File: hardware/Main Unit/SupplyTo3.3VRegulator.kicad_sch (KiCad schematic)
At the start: 22 parts, among them U15 INA180A3, U16 TPS56A37RPAR

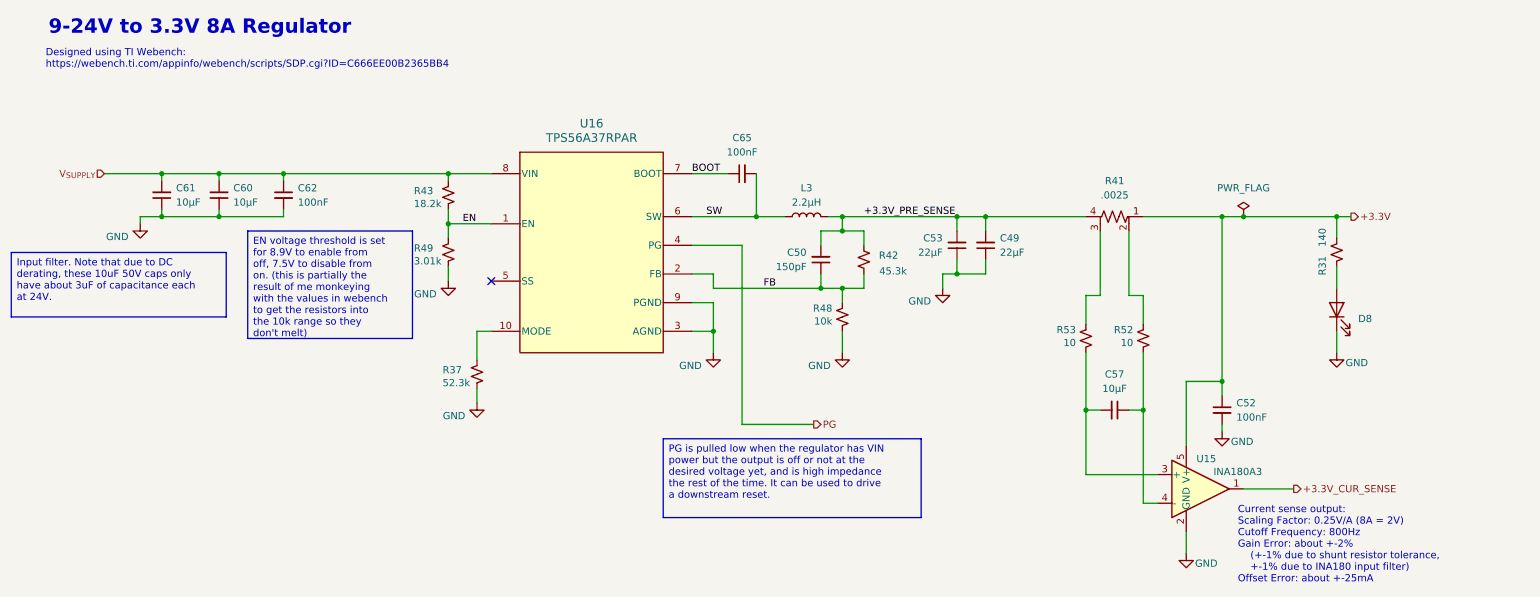
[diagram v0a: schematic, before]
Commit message: Update main unit to KiCAD 10, add clock buffer
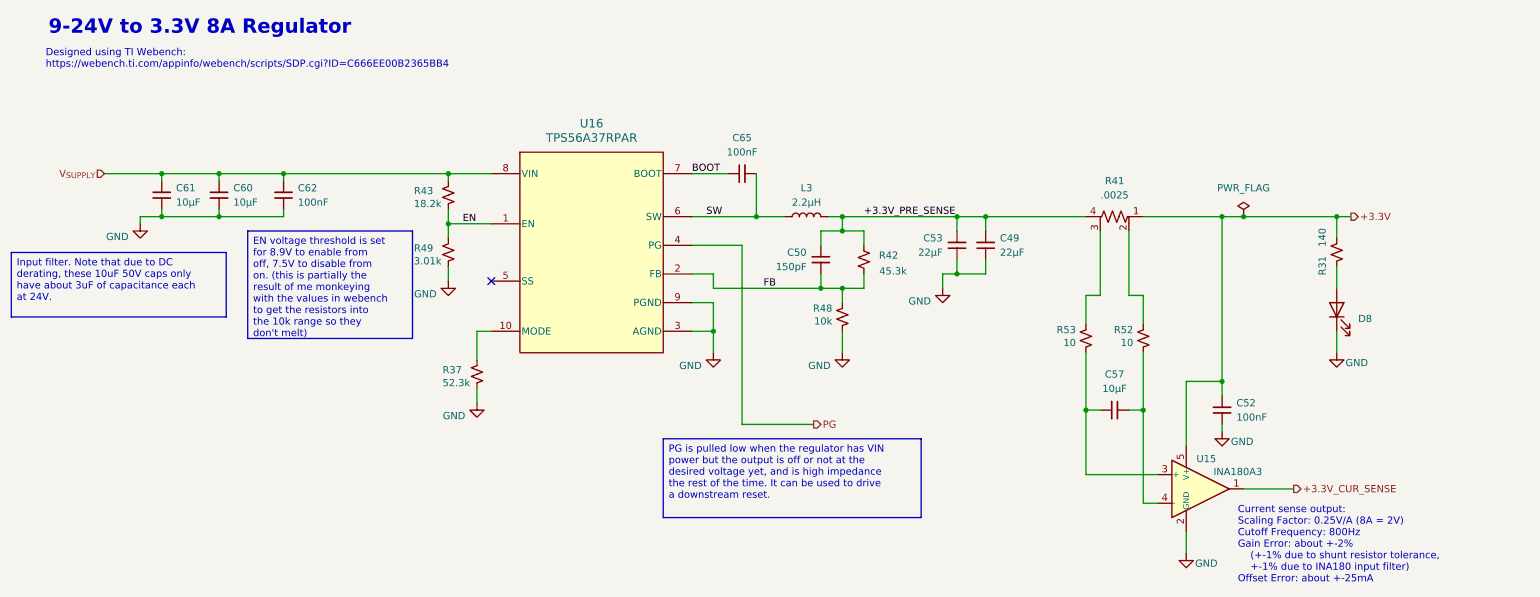
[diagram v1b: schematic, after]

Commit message: Oops forgot to save
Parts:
- C51: renamed from C50; KiLib_Generator (none) -> Digi-Key
- C52: renamed from C49; KiLib_Generator (none) -> Digi-Key
- C54: renamed from C52; KiLib_Generator (none) -> Digi-Key
- C55: renamed from C53; KiLib_Generator (none) -> Digi-Key
- C60: renamed from C57; KiLib_Generator (none) -> Digi-Key
- C62: renamed from C60; KiLib_Generator (none) -> Digi-Key
- C63: renamed from C61; KiLib_Generator (none) -> Digi-Key
- C64: renamed from C62; KiLib_Generator (none) -> Digi-Key
- C67: renamed from C65; KiLib_Generator (none) -> Digi-Key
- R31: KiLib_Generator (none) -> Digi-Key
- R39: renamed from R37; KiLib_Generator (none) -> Digi-Key
- R41: renamed from R42; KiLib_Generator (none) -> Digi-Key
- R42: renamed from R43; KiLib_Generator (none) -> Digi-Key
- R50: renamed from R48; KiLib_Generator (none) -> Digi-Key
- R51: renamed from R49; KiLib_Generator (none) -> Digi-Key
- R55: renamed from R52; KiLib_Generator (none) -> Digi-Key
- R56: renamed from R53; KiLib_Generator (none) -> Digi-Key
- U17: renamed from U15; KiLib_Generator (none) -> Digi-Key
- renumbered R41 to R45, U16 to U18
